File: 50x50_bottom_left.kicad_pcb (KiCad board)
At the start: 2 copper layers, 48.9 x 48.3 mm, 105 parts, among them CON1 BARREL_JACK, J1 INTERCONNECT_1X03, J10 INTERCONNECT_1X03, J11 INTERCONNECT_1X03, J12 INTERCONNECT_1X03, J13 INTERCONNECT_1X03, J14 INTERCONNECT_1X03, J15 INTERCONNECT_1X03, J16 INTERCONNECT_1X03, J17 INTERCONNECT_1X03, J18 INTERCONNECT_1X03, J19 INTERCONNECT_1X03, J2 INTERCONNECT_1X03, J20 INTERCONNECT_1X03, J21 INTERCONNECT_1X03, J22 INTERCONNECT_1X03, J23 INTERCONNECT_1X03, J24 INTERCONNECT_1X03, J25 INTERCONNECT_1X03, J26 INTERCONNECT_1X03, J27 INTERCONNECT_1X03, J28 INTERCONNECT_1X03, J29 INTERCONNECT_1X03, J3 INTERCONNECT_1X03, J30 INTERCONNECT_1X03, J31 INTERCONNECT_1X03, J32 INTERCONNECT_1X03, J33 INTERCONNECT_1X03, J34 INTERCONNECT_1X03, J35 INTERCONNECT_1X03, J36 INTERCONNECT_1X03, J37 INTERCONNECT_1X03, J38 INTERCONNECT_1X03, J39 INTERCONNECT_1X03, J4 INTERCONNECT_1X03, J40 INTERCONNECT_1X03, J41 INTERCONNECT_1X03, J42 INTERCONNECT_1X03, J43 INTERCONNECT_1X03, J44 INTERCONNECT_1X03, J45 INTERCONNECT_1X03, J46 INTERCONNECT_1X03, J47 INTERCONNECT_1X03, J48 INTERCONNECT_1X03, J49 INTERCONNECT_1X03, J5 INTERCONNECT_1X03, J50 INTERCONNECT_1X03, J51 INTERCONNECT_1X03, J52 INTERCONNECT_1X03, J53 INTERCONNECT_1X03, J54 INTERCONNECT_1X03, J55 INTERCONNECT_1X03, J56 INTERCONNECT_1X03, J57 INTERCONNECT_1X03, J58 INTERCONNECT_1X03, J59 INTERCONNECT_1X03, J6 INTERCONNECT_1X03, J60 INTERCONNECT_1X03, J61 INTERCONNECT_1X03, J62 INTERCONNECT_1X03, J63 INTERCONNECT_1X03, J64 INTERCONNECT_1X03, J65 INTERCONNECT_1X02, J7 INTERCONNECT_1X03, J8 INTERCONNECT_1X03, J9 INTERCONNECT_1X03, P1 CONN_6X2, P2 CONN_6X2, U1 LM7805CT

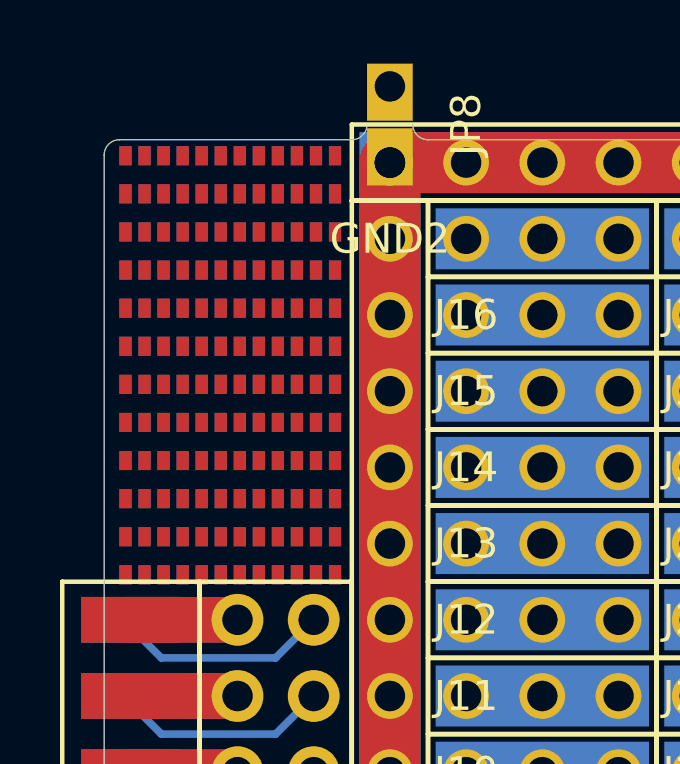
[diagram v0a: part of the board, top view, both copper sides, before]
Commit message: increased pad size for SMD grid on bottom-left quarter
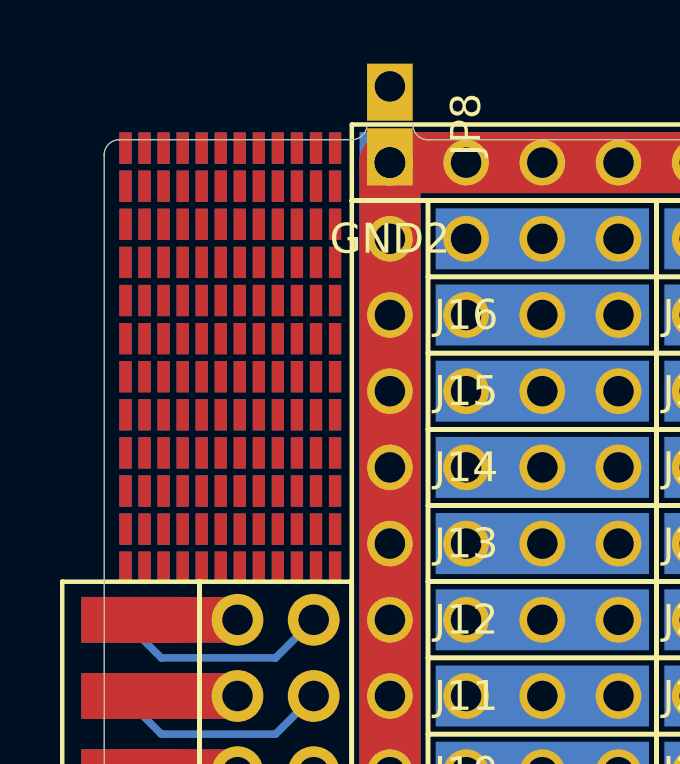
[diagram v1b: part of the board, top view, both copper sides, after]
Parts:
- moved Ref** 0.25 mm to (46.1, 42.1) (x2)
- moved Ref** 0.25 mm to (46.1, 37.0) (x2)
- moved Ref** 0.25 mm to (46.1, 31.9) (x2)

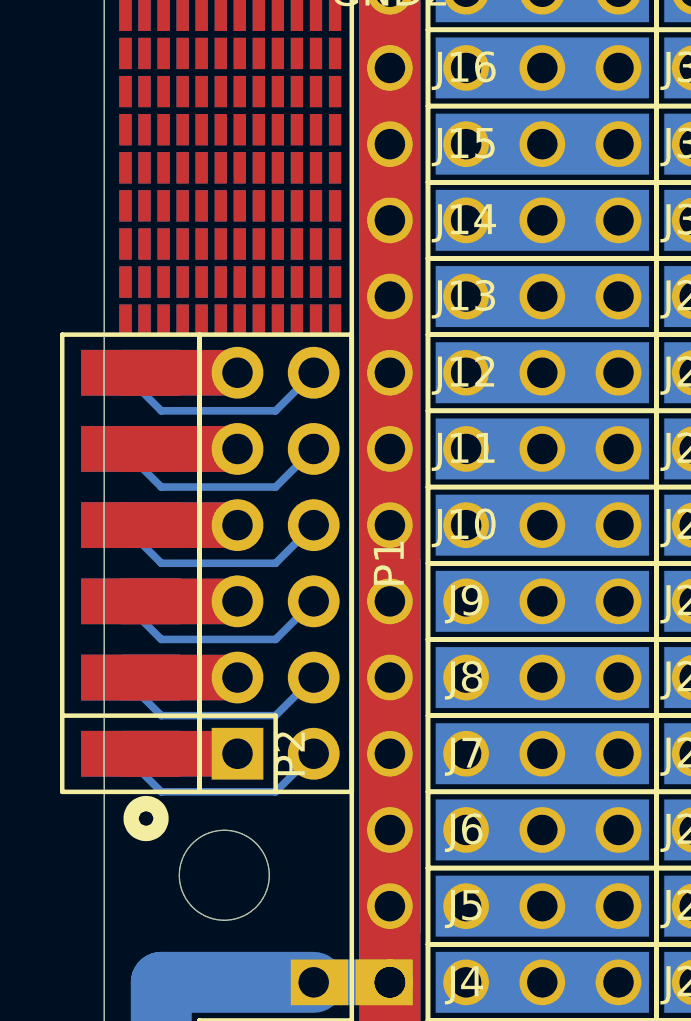
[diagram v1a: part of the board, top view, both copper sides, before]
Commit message: increased .1" edge connector from 2*6 to 2*8 to account for the A-100 system bus used in modular synthesizers
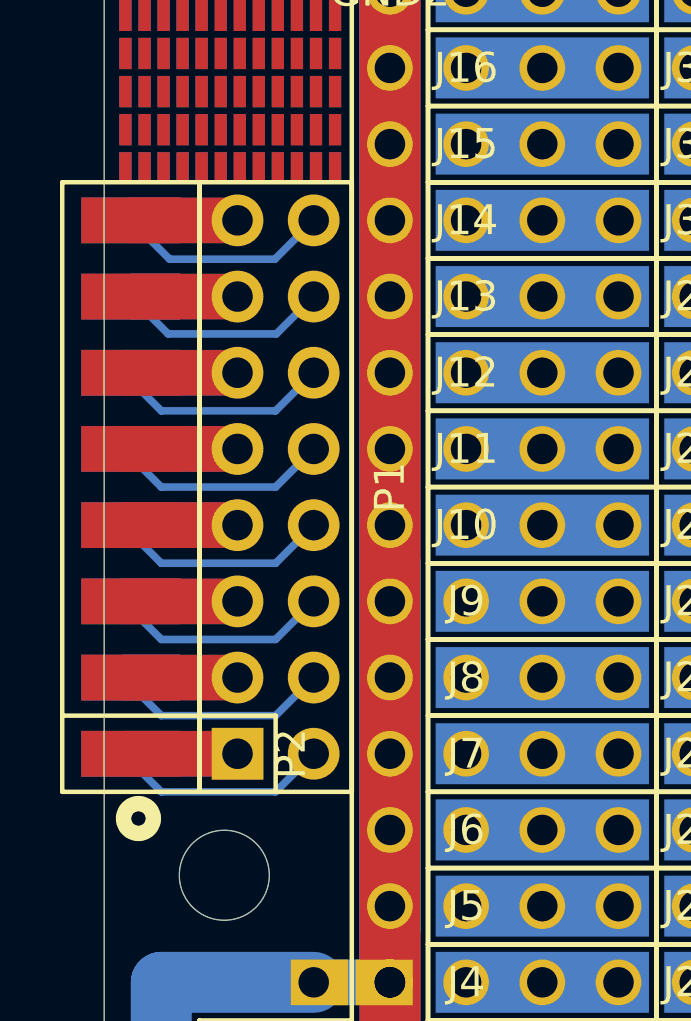
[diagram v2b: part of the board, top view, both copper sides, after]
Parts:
- removed the Ref** at (46.1, 42.1) (x2)
- P1: value CONN_6X2 -> CONN_8X2; footprint Socket_Strips:Socket_Strip_Straight_2x06 -> Socket_Strips:Socket_Strip_Straight_2x08
- P2: value CONN_6X2 -> CONN_8X2; footprint 2.54mm_Pin_Headers:Edge_2x06 -> 2.54mm_Pin_Headers:Edge_2x08
- moved P1 2.54 mm to (48.3, 49.5)
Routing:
- net Net-(P1-Pad16): track 0.00 -> 8.06 mm
- net Net-(P1-Pad14): track 0.00 -> 8.02 mm
- net Net-(P1-Pad15): track 0.00 -> 3.56 mm
- net Net-(P1-Pad13): track 0.00 -> 3.56 mm

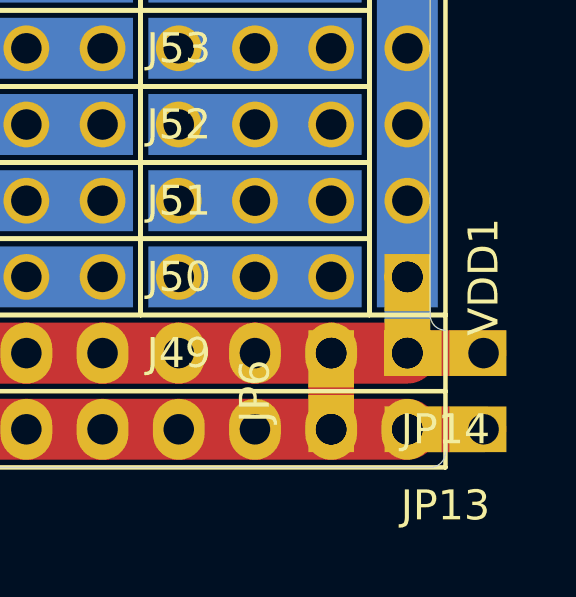
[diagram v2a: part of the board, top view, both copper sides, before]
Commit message: flipped the outermost power rail solder jumper, so that all of these solder-jumpers are shorted on the front
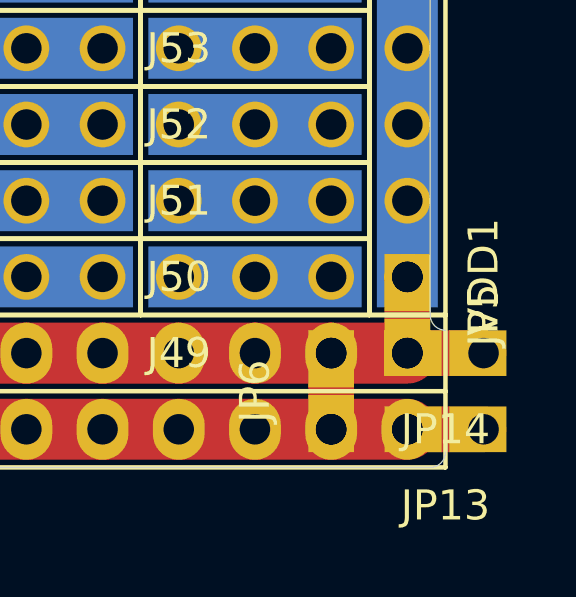
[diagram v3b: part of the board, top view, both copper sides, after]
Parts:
- JP5: moved to F.Cu
- turned JP5 to 90 degrees

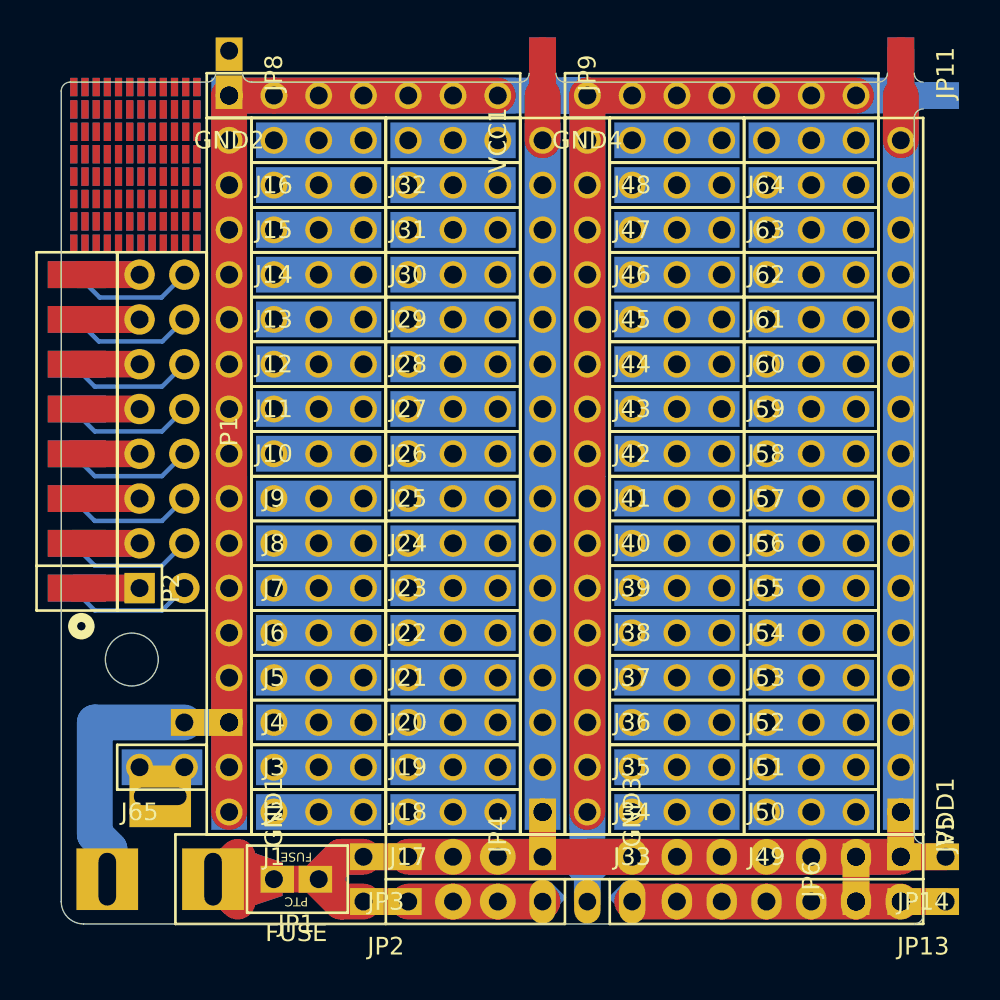
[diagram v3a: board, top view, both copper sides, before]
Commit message: rounded some corners
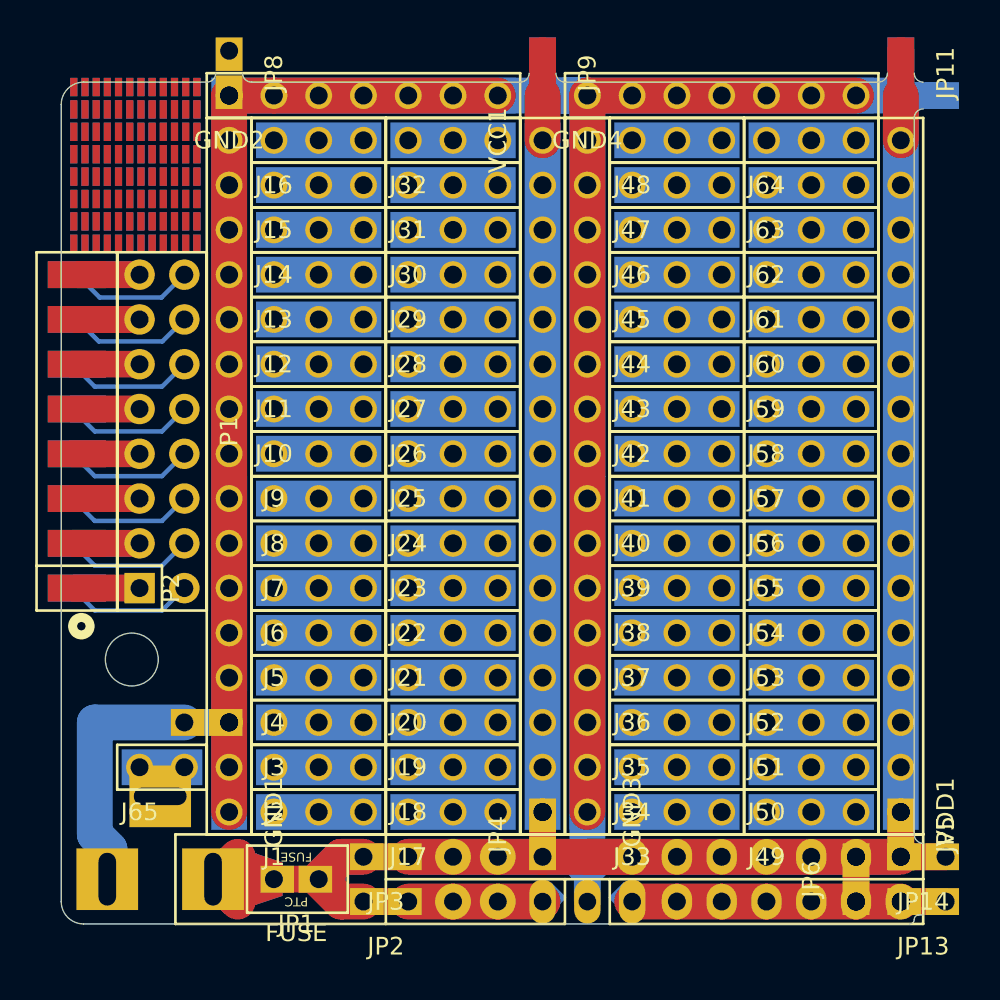
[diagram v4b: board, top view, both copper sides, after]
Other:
- outline, holes or cut-outs redrawn

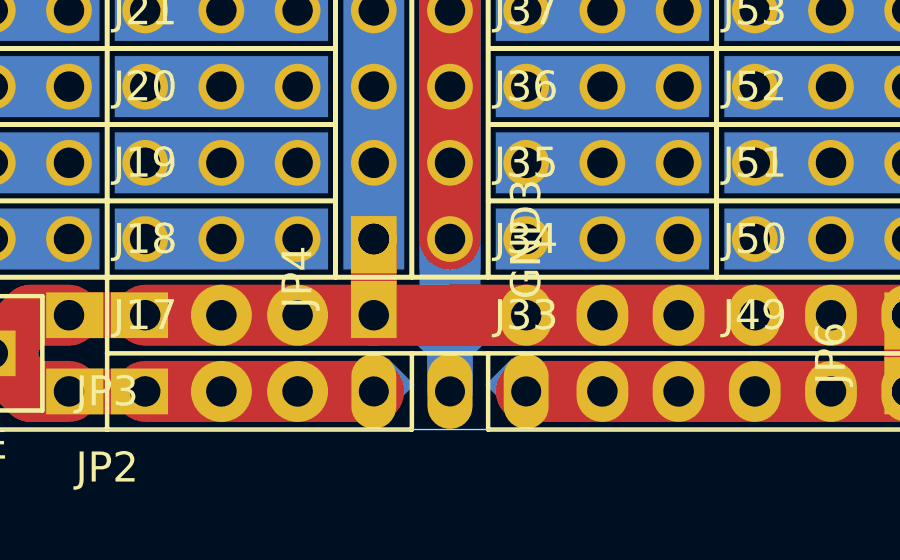
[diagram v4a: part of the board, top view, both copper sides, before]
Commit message: increased the size of 78XX capacitor values, so that they are readable and flipped 78XX text on bottom left so that it does not conflict with capacitor pads
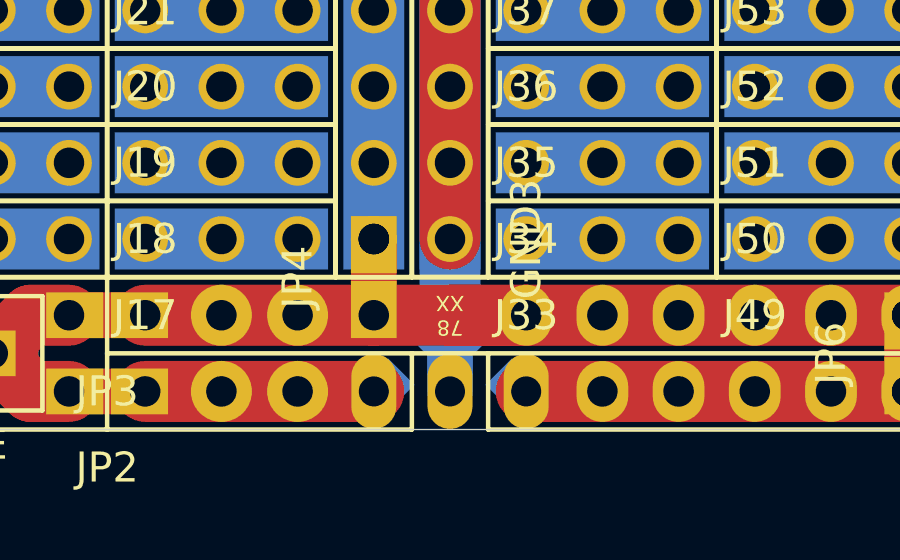
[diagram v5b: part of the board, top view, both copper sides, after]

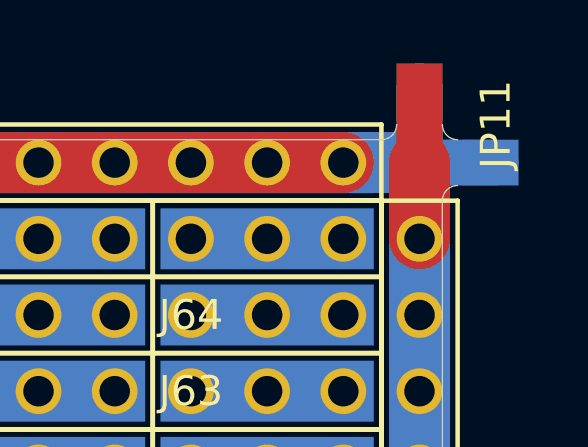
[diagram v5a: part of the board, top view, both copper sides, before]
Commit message: remove center border outline, because drilling it plated shorts PWR and GND
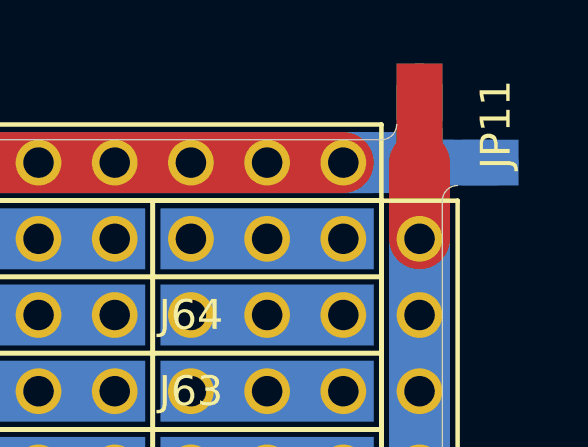
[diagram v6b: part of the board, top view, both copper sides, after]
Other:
- outline, holes or cut-outs redrawn
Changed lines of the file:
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@@
-(kicad_pcb (version 4) (host pcbnew "(2015-01-08 BZR 5360)-product")
+(kicad_pcb (version 4) (host pcbnew 4.0.2-stable)
   (general
     (links 341)
     (no_connects 6)
-    (area 34.144048 26.7335 95.967572 82.309)
+    (area 37.128379 24.905285 94.697572 82.309)
     (thickness 1.6)
-    (drawings 54)
+    (drawings 53)
     (tracks 88)
     (zones 0)
@@
   (gr_line (start 88.9 29.718) (end 71.12 29.718) (angle 90) (layer Edge.Cuts) (width 0.0254))
   (gr_arc (start 88.9 29.21) (end 88.9 29.718) (angle -90) (layer Edge.Cuts) (width 0.0254))
-  (gr_arc (start 91.44 29.21) (end 90.932 29.21) (angle -90) (layer Edge.Cuts) (width 0.0254))
   (gr_arc (start 91.44 31.75) (end 91.44 31.242) (angle -90) (layer Edge.Cuts) (width 0.0254))
   (gr_line (start 90.932 72.39) (end 90.932 31.75) (angle 90) (layer Edge.Cuts) (width 0.0254))
